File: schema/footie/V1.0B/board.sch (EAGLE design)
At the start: 38 parts, among them T1 2N3565, U2 USD-SOCKETNEW, U3 HC_05, U4 MCP73831, U5 3.3 regulator, U6 ATMEGA328P-AU

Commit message: fix version 1.0B
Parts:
- removed JP1: RA 6Pin SMD, SparkFun-Connectors:M06SMD
- added U$2: JST_VERTICAL, SparkFun-Connectors:JST_VERTICAL
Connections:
- net +3V3: now also U$2.4; no longer JP1.4
- net ARDUINO_RX: now also U$2.6; no longer JP1.6
- net ARDUINO_TX: now also U$2.5; no longer JP1.5
- net DTR: now also U$2.2; no longer JP1.2
- net GND: now also U$2.3; no longer JP1.3
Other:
- note added: "1.0B"
- note added: "ARDUINO"
- note added: "BLUETOOTH"
- note added: "CHARGER"
- note added: "FOOTI"
- note added: "GPS"
- note added: "PROGRAM"
- note added: "RGB LED"
- note added: "SWITCH BUTTONS"
- note added: "USB CONNECTOR#"
- note added: "VOLTAGE REGULATOR"
- moved on the sheet: BATTERY_CONNECTOR, C1, C10, C11, C2, C3, C4, C8, C9, D1, D2, EEPROM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

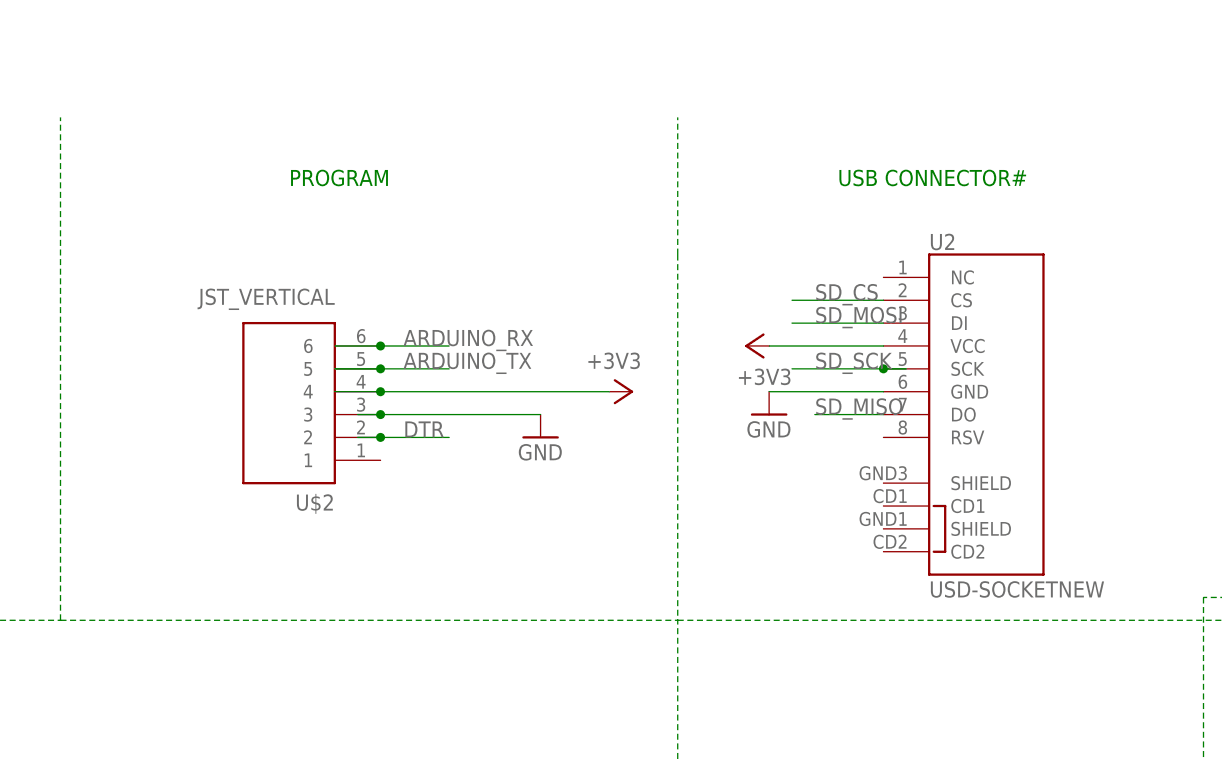
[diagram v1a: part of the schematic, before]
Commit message: fix sdcard position add autoreset capacitor
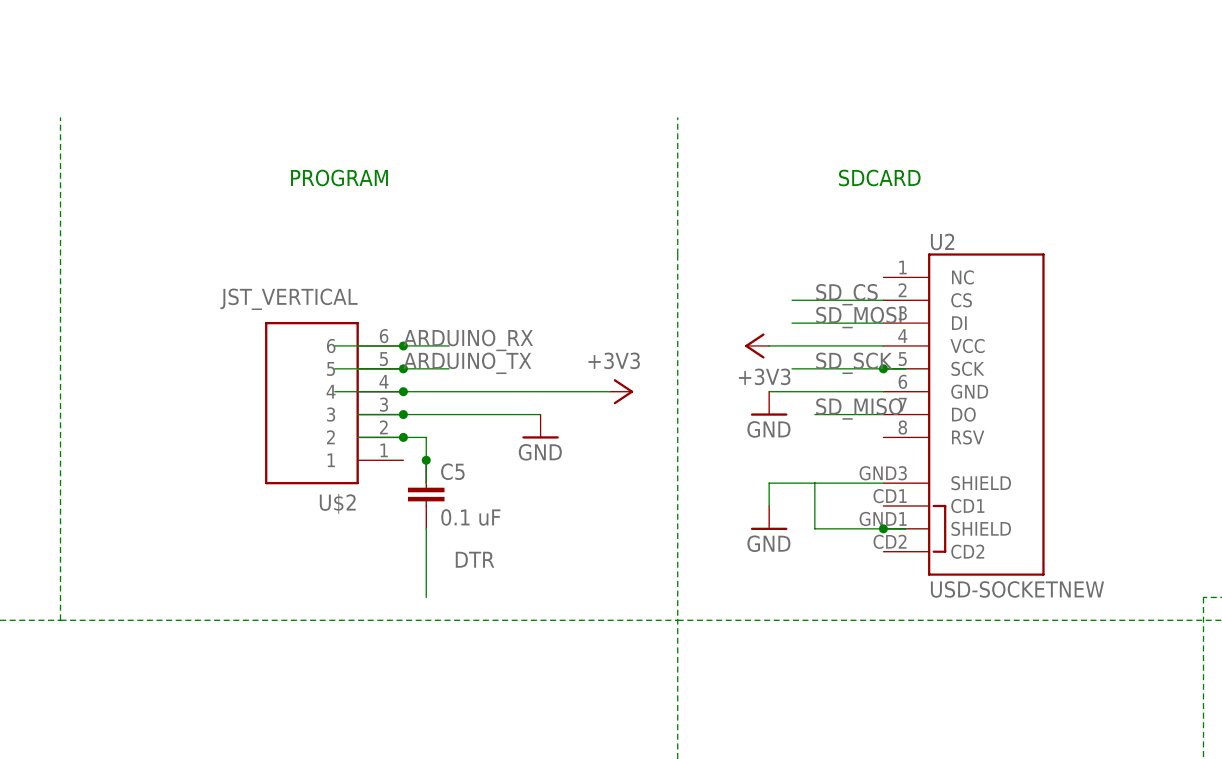
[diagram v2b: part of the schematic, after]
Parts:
- added C5: 0.1 uF, SparkFun-Capacitors:CAP1206
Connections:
- new net N$13: C5.1, U$2.2
- net DTR: now also C5.2; no longer U$2.2
- net GND: now also U2.SHIELD@1, U2.SHIELD@3
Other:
- note added: "SDCARD"
- note removed: "USB CONNECTOR#"
- moved on the sheet: U$2
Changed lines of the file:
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@@
 <part name="GND11" library="supply1" deviceset="GND" device=""/>
 <part name="+3V8" library="supply1" deviceset="+3V3" device=""/>
+<part name="GND18" library="supply1" deviceset="GND" device=""/>
+<part name="C5" library="SparkFun-Capacitors" deviceset="CAP" device="1206" value="0.1 uF"/>
 </parts>
 <sheets>
@@
 <text x="106.68" y="203.2" size="1.778" layer="91">PROGRAM</text>
 <text x="124.46" y="177.8" size="1.778" layer="91">PROGRAM</text>
-<text x="185.42" y="177.8" size="1.778" layer="91">USB CONNECTOR#</text>
+<text x="185.42" y="177.8" size="1.778" layer="91">SDCARD</text>
 <text x="284.48" y="177.8" size="1.778" layer="91">CHARGER</text>
 <text x="269.24" y="116.84" size="1.778" layer="91">VOLTAGE REGULATOR</text>
@@
 <instance part="FRAME2" gate="G$1" x="-20.32" y="-91.44"/>
 <instance part="FRAME2" gate="G$2" x="246.38" y="-91.44"/>
-<instance part="U$2" gate="G$1" x="121.92" y="152.4" rot="R180"/>
+<instance part="U$2" gate="G$1" x="124.46" y="152.4" rot="R180"/>
 <instance part="GND11" gate="1" x="152.4" y="149.86"/>
 <instance part="+3V8" gate="G$1" x="162.56" y="154.94" rot="R270"/>
+<instance part="GND18" gate="1" x="177.8" y="139.7"/>
+<instance part="C5" gate="G$1" x="139.7" y="142.24"/>
 </instances>
 <busses>
@@
 </segment>
 <segment>
-<wire x1="129.54" y1="154.94" x2="134.62" y2="154.94" width="0.1524" layer="91"/>
+<wire x1="129.54" y1="154.94" x2="137.16" y2="154.94" width="0.1524" layer="91"/>
 <pinref part="+3V8" gate="G$1" pin="+3V3"/>
 <pinref part="U$2" gate="G$1" pin="4"/>
-<wire x1="134.62" y1="154.94" x2="160.02" y2="154.94" width="0.1524" layer="91"/>
-<junction x="134.62" y="154.94"/>
+<wire x1="137.16" y1="154.94" x2="160.02" y2="154.94" width="0.1524" layer="91"/>
+<junction x="137.16" y="154.94"/>
 </segment>
 </net>
@@
 </segment>
 <segment>
-<wire x1="129.54" y1="157.48" x2="134.62" y2="157.48" width="0.1524" layer="91"/>
+<wire x1="129.54" y1="157.48" x2="137.16" y2="157.48" width="0.1524" layer="91"/>
 <pinref part="U$2" gate="G$1" pin="5"/>
-<wire x1="134.62" y1="157.48" x2="142.24" y2="157.48" width="0.1524" layer="91"/>
-<junction x="134.62" y="157.48"/>
+<wire x1="137.16" y1="157.48" x2="142.24" y2="157.48" width="0.1524" layer="91"/>
+<junction x="137.16" y="157.48"/>
 <label x="137.16" y="157.48" size="1.778" layer="95"/>
 </segment>
@@
 </segment>
 <segment>
-<wire x1="129.54" y1="160.02" x2="134.62" y2="160.02" width="0.1524" layer="91"/>
+<wire x1="129.54" y1="160.02" x2="137.16" y2="160.02" width="0.1524" layer="91"/>
 <pinref part="U$2" gate="G$1" pin="6"/>
-<wire x1="134.62" y1="160.02" x2="142.24" y2="160.02" width="0.1524" layer="91"/>
-<junction x="134.62" y="160.02"/>
+<wire x1="137.16" y1="160.02" x2="142.24" y2="160.02" width="0.1524" layer="91"/>
+<junction x="137.16" y="160.02"/>
 <label x="137.16" y="160.02" size="1.778" layer="95"/>
 </segment>
@@
 </segment>
 <segment>
-<wire x1="132.08" y1="149.86" x2="134.62" y2="149.86" width="0.1524" layer="91"/>
-<pinref part="U$2" gate="G$1" pin="2"/>
-<wire x1="134.62" y1="149.86" x2="142.24" y2="149.86" width="0.1524" layer="91"/>
-<junction x="134.62" y="149.86"/>
-<label x="137.16" y="149.86" size="1.778" layer="95"/>
+<pinref part="C5" gate="G$1" pin="2"/>
+<wire x1="139.7" y1="139.7" x2="139.7" y2="132.08" width="0.1524" layer="91"/>
+<label x="147.32" y="137.16" size="1.778" layer="95" rot="R180"/>
 </segment>
 </net>
@@
 </segment>
 <segment>
-<wire x1="132.08" y1="152.4" x2="134.62" y2="152.4" width="0.1524" layer="91"/>
+<wire x1="132.08" y1="152.4" x2="137.16" y2="152.4" width="0.1524" layer="91"/>
 <pinref part="GND11" gate="1" pin="GND"/>
 <pinref part="U$2" gate="G$1" pin="3"/>
-<wire x1="134.62" y1="152.4" x2="152.4" y2="152.4" width="0.1524" layer="91"/>
-<junction x="134.62" y="152.4"/>
+<wire x1="137.16" y1="152.4" x2="152.4" y2="152.4" width="0.1524" layer="91"/>
+<junction x="137.16" y="152.4"/>
+</segment>
+<segment>
+<pinref part="U2" gate="G$1" pin="SHIELD@1"/>
+<pinref part="GND18" gate="1" pin="GND"/>
+<wire x1="190.5" y1="144.78" x2="182.88" y2="144.78" width="0.1524" layer="91"/>
+<wire x1="182.88" y1="144.78" x2="177.8" y2="144.78" width="0.1524" layer="91"/>
+<wire x1="177.8" y1="144.78" x2="177.8" y2="142.24" width="0.1524" layer="91"/>
+<wire x1="193.04" y1="139.7" x2="190.5" y2="139.7" width="0.1524" layer="91"/>
+<wire x1="190.5" y1="139.7" x2="182.88" y2="139.7" width="0.1524" layer="91"/>
+<wire x1="182.88" y1="139.7" x2="182.88" y2="144.78" width="0.1524" layer="91"/>
+<pinref part="U2" gate="G$1" pin="SHIELD@3"/>
+<junction x="190.5" y="139.7"/>
 </segment>
 </net>
@@
 </segment>
 </net>
+<net name="N$13" class="0">
+<segment>
+<wire x1="132.08" y1="149.86" x2="137.16" y2="149.86" width="0.1524" layer="91"/>
+<wire x1="137.16" y1="149.86" x2="139.7" y2="149.86" width="0.1524" layer="91"/>
+<wire x1="139.7" y1="149.86" x2="139.7" y2="147.32" width="0.1524" layer="91"/>
+<pinref part="U$2" gate="G$1" pin="2"/>
+<junction x="137.16" y="149.86"/>
+<pinref part="C5" gate="G$1" pin="1"/>
+<wire x1="139.7" y1="147.32" x2="139.7" y2="144.78" width="0.1524" layer="91"/>
+<junction x="139.7" y="147.32"/>
+</segment>
+</net>

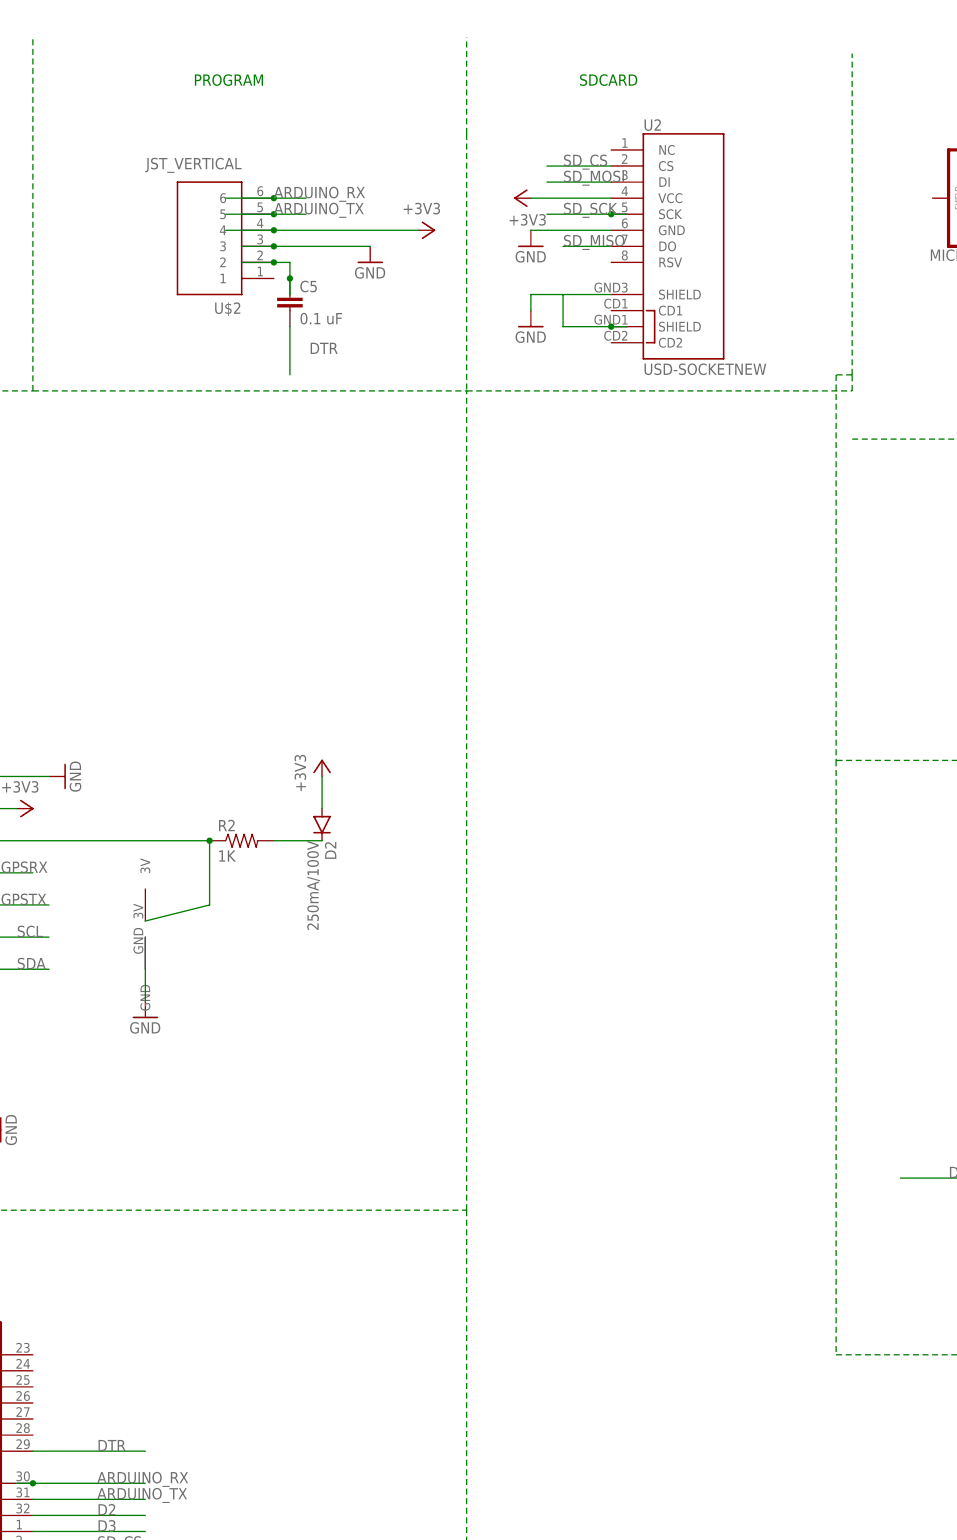
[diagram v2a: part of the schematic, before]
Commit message: add fix for reset add fix for sdcard add gerber files
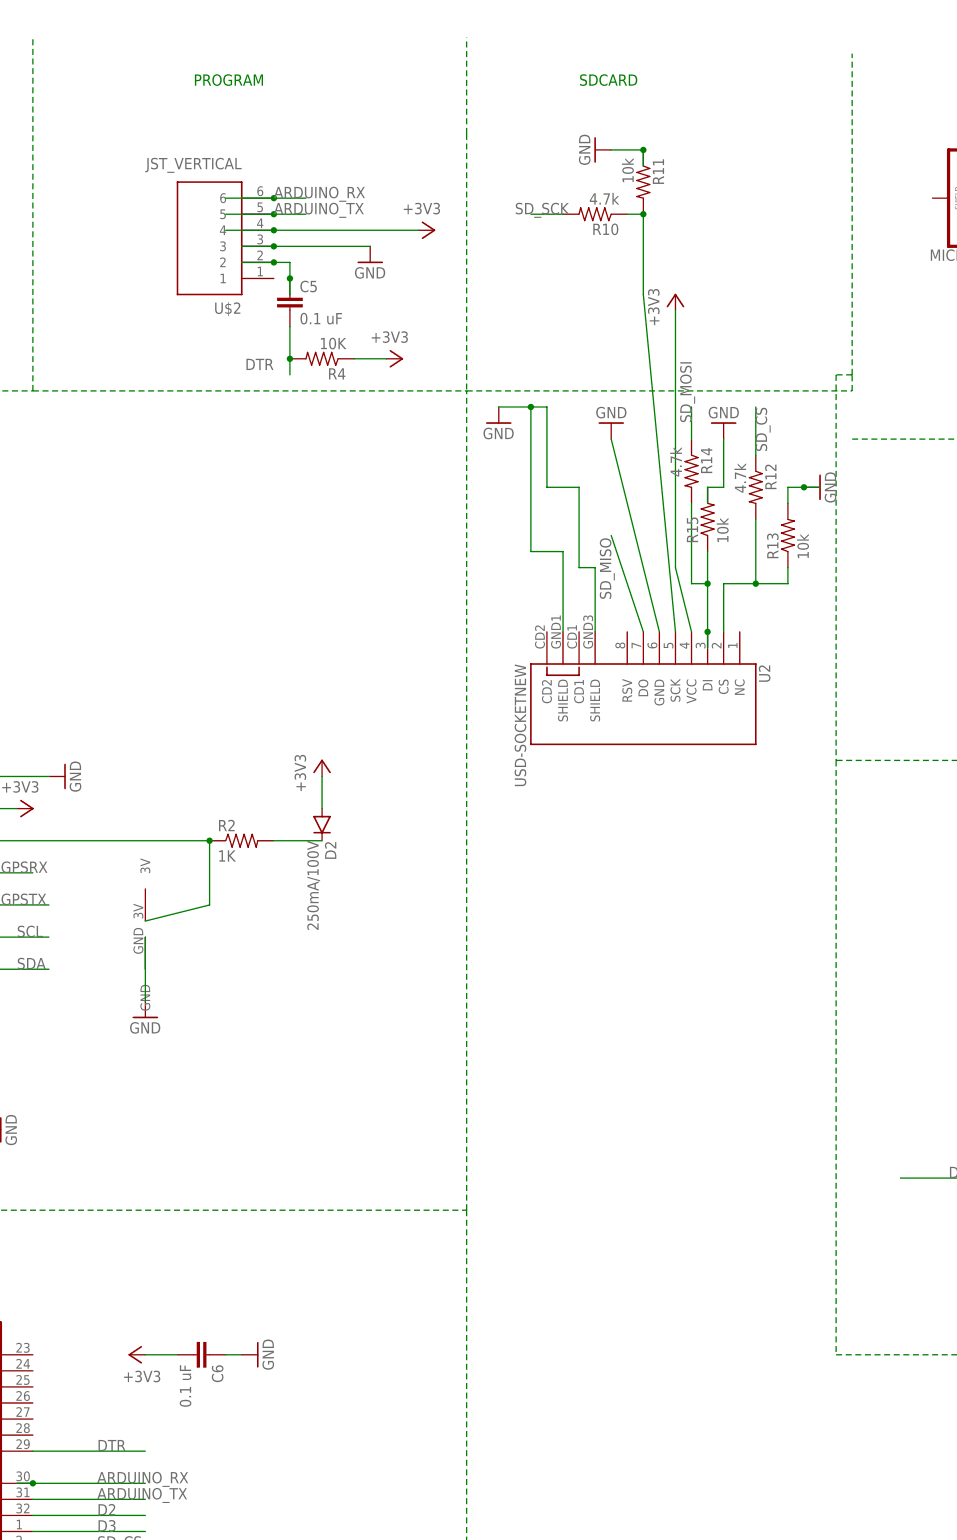
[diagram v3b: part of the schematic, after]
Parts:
- added C6: 0.1 uF, SparkFun-Capacitors:CAP1206
- added R10, R12, R14: 4.7k, SparkFun-Passives:RESISTOR1206
- added R11, R13, R15: 10k, SparkFun-Passives:RESISTOR1206
- added R4: 10K, SparkFun-Passives:RESISTOR1206
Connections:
- new net N$14: R10.1, R11.2, U2.SCK
- new net N$17: R12.2, R13.1, U2.CS
- new net N$26: R14.2, R15.1, U2.DI
- net +3V3: now also C6.2, R4.1
- net DTR: now also R4.2
- net GND: now also C6.1, R11.1, R13.2, R15.2
- net SD_CS: now also R12.1; no longer U2.CS
- net SD_MOSI: now also R14.1; no longer U2.DI
- net SD_SCK: now also R10.2; no longer U2.SCK
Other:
- moved on the sheet: U2
